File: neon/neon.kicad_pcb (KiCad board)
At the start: 2 copper layers, 60 x 50 mm, 30 parts, among them J1 V3V3-VIO, J2 V3V3-GND, J3 V3V3-GND, J4 V3V3-GND, J5 VBUS-VCC, U1 FT4232H_module, U2 A, U3 B, U4 C, U5 D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

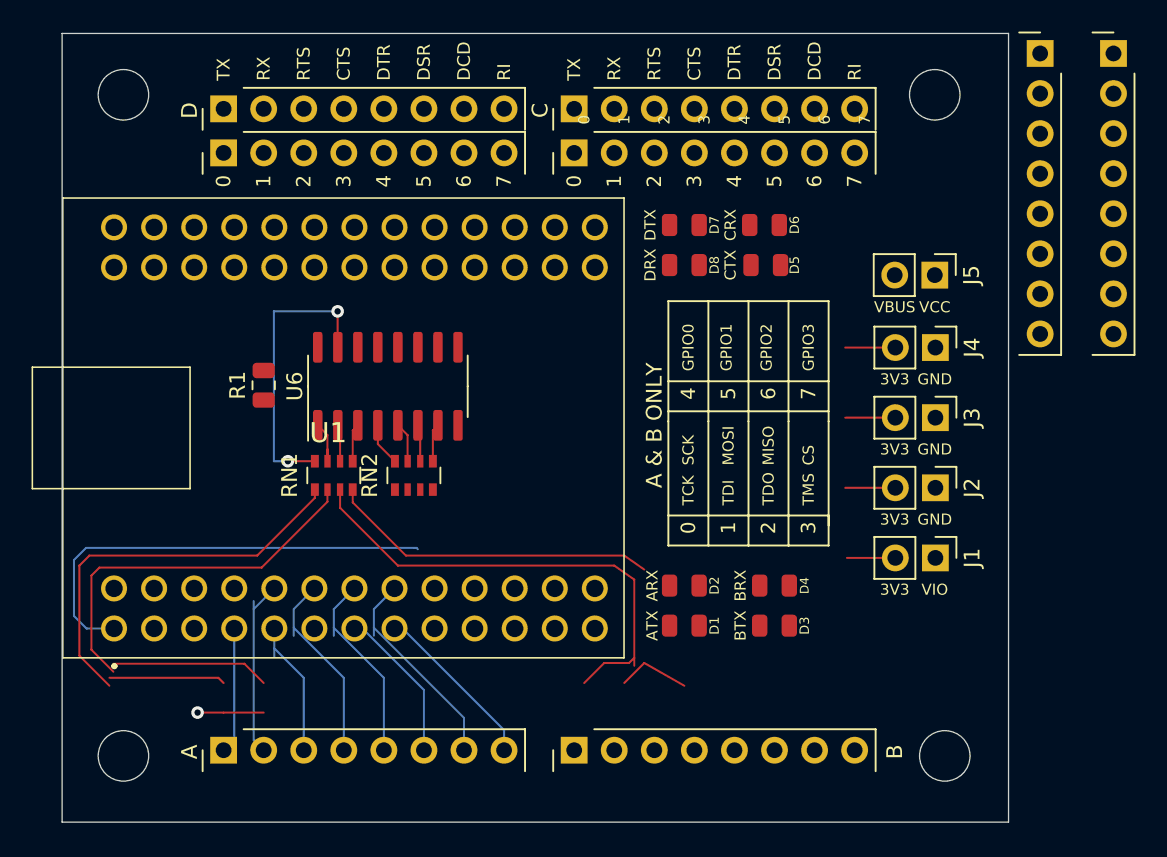
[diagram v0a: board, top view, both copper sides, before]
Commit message: All sniffers on PCB
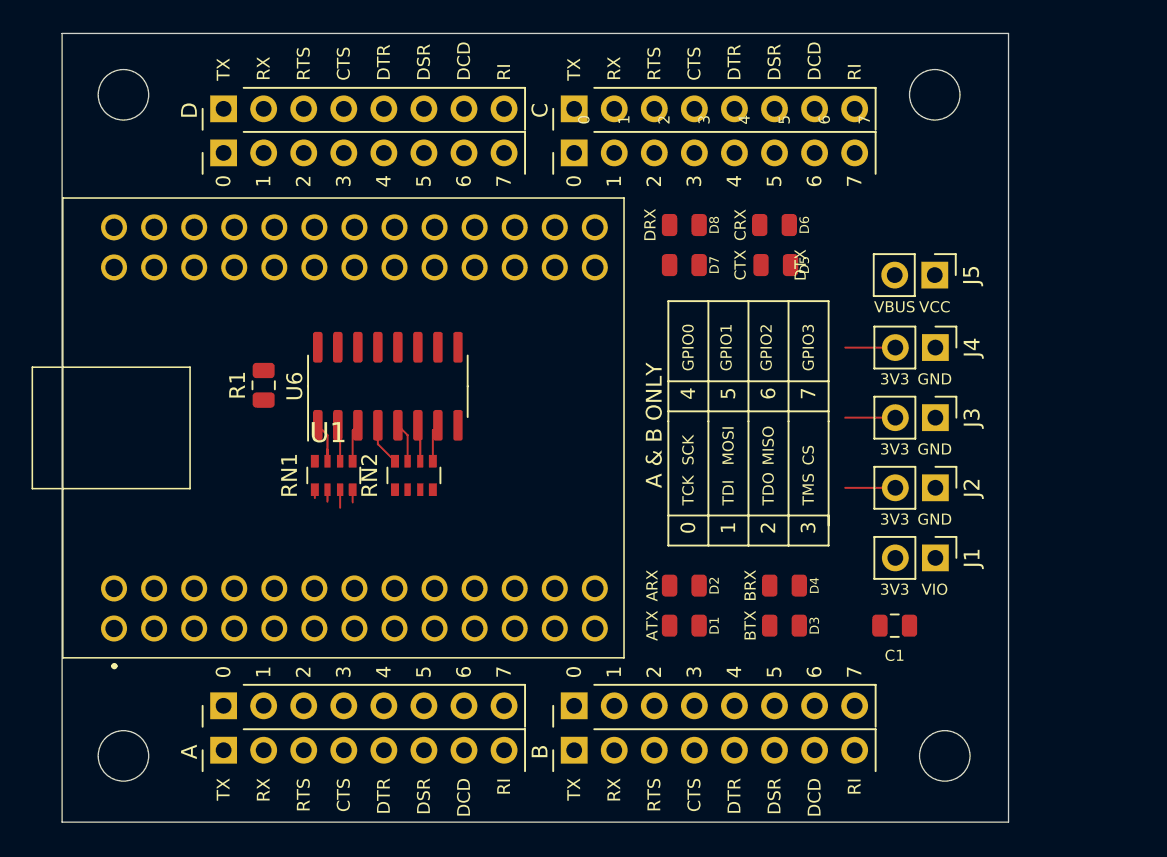
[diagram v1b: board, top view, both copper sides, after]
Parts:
- added C1: 100nF, Capacitor_SMD:C_0805_2012Metric, F.Cu at (168.3, 117.5)
- moved S3 66.3 mm to (125.7, 122.6), turned to 90 degrees
- moved S4 53.7 mm to (148.0, 122.6), turned to 90 degrees
- moved D7 2.54 mm to (154.9, 94.6)
- moved D8 2.54 mm to (154.9, 92.1)
- moved D5 0.64 mm to (160.7, 94.6)
- moved D3 0.63 mm to (161.3, 117.5)
- moved D4 0.63 mm to (161.3, 114.9)
- moved D6 0.63 mm to (160.7, 92.1)
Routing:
- net Net-(D2-Pad2): track 34.4 -> 0.77 mm
- net Net-(D1-Pad2): track 33.0 -> 0.53 mm
- net V3V3: track 41.2 -> 9.53 mm
- net Net-(D3-Pad2): track 30.9 -> 1.15 mm
- net Net-(D4-Pad2): track 25.7 -> 0.81 mm
- net Net-(RN1-Pad8): track 18.4 -> 0.02 mm, vias 2 -> 0
- net /FT4232H.sch/AD6: track 13.7 -> 0.00 mm
- net /FT4232H.sch/AD4: track 12.6 -> 0.00 mm
- net /FT4232H.sch/AD3: track 12.6 -> 0.00 mm
- net /FT4232H.sch/AD7: track 11.9 -> 0.00 mm
- net /FT4232H.sch/AD1: track 11.8 -> 0.00 mm
- net /FT4232H.sch/AD5: track 10.0 -> 0.00 mm
- net /FT4232H.sch/AD2: track 9.00 -> 0.00 mm
- net /FT4232H.sch/AD0: track 8.50 -> 0.00 mm
- net GND: track 4.19 -> 0.00 mm, vias 1 -> 0

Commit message: Fixes
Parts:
- moved D6 0.63 mm to (161.3, 92.1)
- moved D5 0.51 mm to (161.2, 94.6)
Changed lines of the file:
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@@
     (tags "resistor array")
     (attr smd)
-    (fp_text reference RN1 (at 0 -2.8 90) (layer F.SilkS)
-      (effects (font (size 1 1) (thickness 0.15)))
+    (fp_text reference RN1 (at 0 -2.159 90) (layer F.SilkS)
+      (effects (font (size 0.7 0.7) (thickness 0.15)))
     )
     (fp_text value 330 (at 0 2.8 90) (layer F.Fab)
@@
     (tags "resistor array")
     (attr smd)
-    (fp_text reference RN2 (at 0 -2.8 90) (layer F.SilkS)
-      (effects (font (size 1 1) (thickness 0.15)))
+    (fp_text reference RN2 (at 0 -2.159 90) (layer F.SilkS)
+      (effects (font (size 0.7 0.7) (thickness 0.15)))
     )
     (fp_text value 330 (at 0 2.8 90) (layer F.Fab)
@@
   )
   (module neon_footprints:LED_0805_2012Metric (layer F.Cu)
-    (at 160.655 92.075 180)
+    (at 161.29 92.075 180)
     (descr "LED SMD 0805 (2012 Metric), square (rectangular) end terminal, IPC_7351 nominal, (Body size source: https://docs.google.com/spreadsheets/d/1BsfQQcO9C6DZCsRaXUlFlo91Tg2WpOkGARC1WS5S8t0/edit?usp=sharing), generated with kicad-footprint-generator")
     (tags diode)
@@
   )
   (module neon_footprints:LED_0805_2012Metric (layer F.Cu)
-    (at 160.735 94.615 180)
+    (at 161.243 94.615 180)
     (descr "LED SMD 0805 (2012 Metric), square (rectangular) end terminal, IPC_7351 nominal, (Body size source: https://docs.google.com/spreadsheets/d/1BsfQQcO9C6DZCsRaXUlFlo91Tg2WpOkGARC1WS5S8t0/edit?usp=sharing), generated with kicad-footprint-generator")
     (tags diode)
@@
     (tags "SOIC SO")
     (attr smd)
-    (fp_text reference U6 (at 0 -5.9 90) (layer F.SilkS)
-      (effects (font (size 1 1) (thickness 0.15)))
+    (fp_text reference U6 (at 0.065 -5.588 90) (layer F.SilkS)
+      (effects (font (size 0.7 0.7) (thickness 0.15)))
     )
     (fp_text value 74HC595 (at 0 5.9 90) (layer F.Fab)
@@
     (tags resistor)
     (attr smd)
-    (fp_text reference R1 (at 0 -1.65 90) (layer F.SilkS)
-      (effects (font (size 1 1) (thickness 0.15)))
+    (fp_text reference R1 (at 0 -1.524 90) (layer F.SilkS)
+      (effects (font (size 0.7 0.7) (thickness 0.15)))
     )
     (fp_text value 10k (at 0 1.65 90) (layer F.Fab)
@@
     (effects (font (size 0.7112 0.7112) (thickness 0.175)))
   )
-  (gr_text CRX (at 158.496 92.075 90) (layer F.SilkS)
+  (gr_text CRX (at 159.004 92.075 90) (layer F.SilkS)
     (effects (font (size 0.7112 0.7112) (thickness 0.175)))
   )
@@
     (effects (font (size 0.7112 0.7112) (thickness 0.175)))
   )
-  (gr_text DTX (at 162.306 94.615 90) (layer F.SilkS)
+  (gr_text DTX (at 152.781 94.615 90) (layer F.SilkS)
     (effects (font (size 0.7112 0.7112) (thickness 0.175)))
   )
-  (gr_text CTX (at 158.496 94.615 90) (layer F.SilkS)
+  (gr_text CTX (at 159.004 94.615 90) (layer F.SilkS)
     (effects (font (size 0.7112 0.7112) (thickness 0.175)))
   )

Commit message: Problems fixes
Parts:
- moved C1 0.64 mm to (168.3, 118.1)
- moved J2 0.64 mm to (170.9, 109.4)
- moved J4 0.64 mm to (170.9, 100.5)
- moved J5 0.64 mm to (170.8, 95.9)
- moved J1 0.63 mm to (170.9, 113.8)
- moved J3 0.63 mm to (170.9, 104.9)
- renumbered U4 to U2, U2 to U4

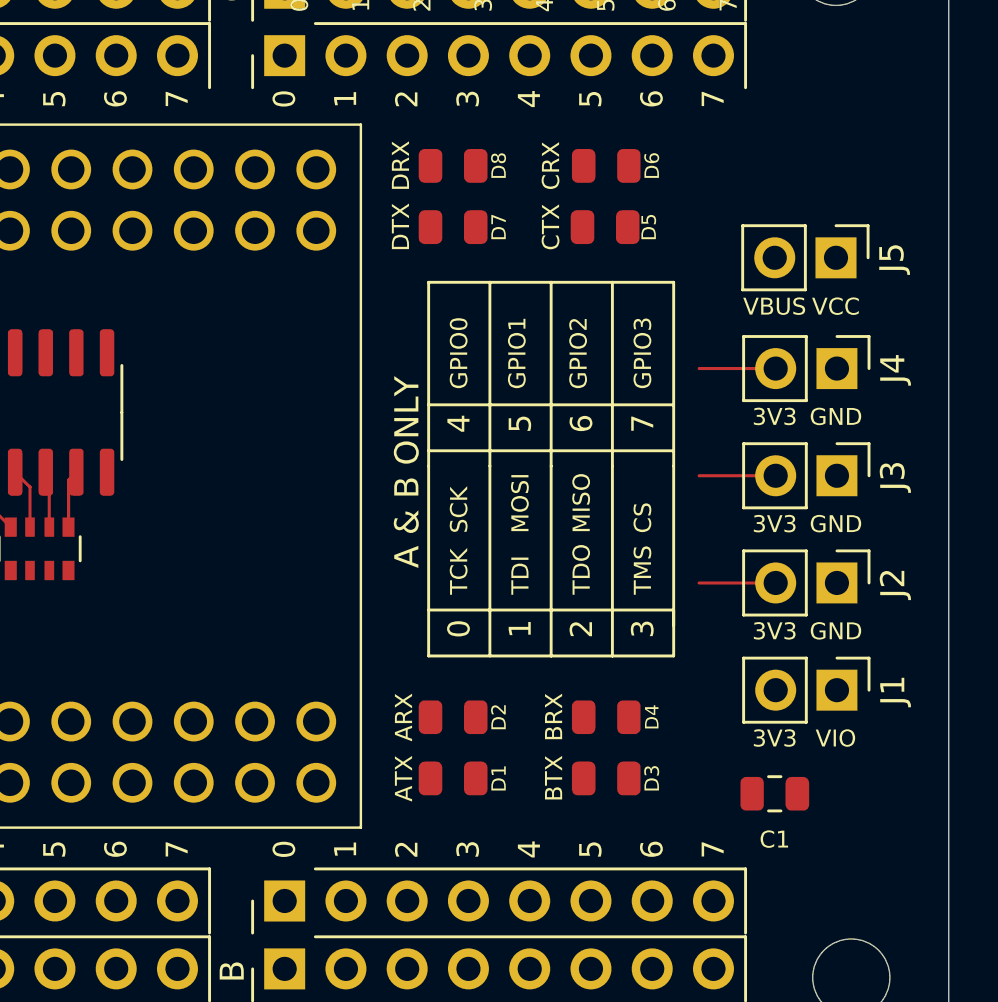
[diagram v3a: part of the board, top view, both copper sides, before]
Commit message: Center things & rotate J1 & J5
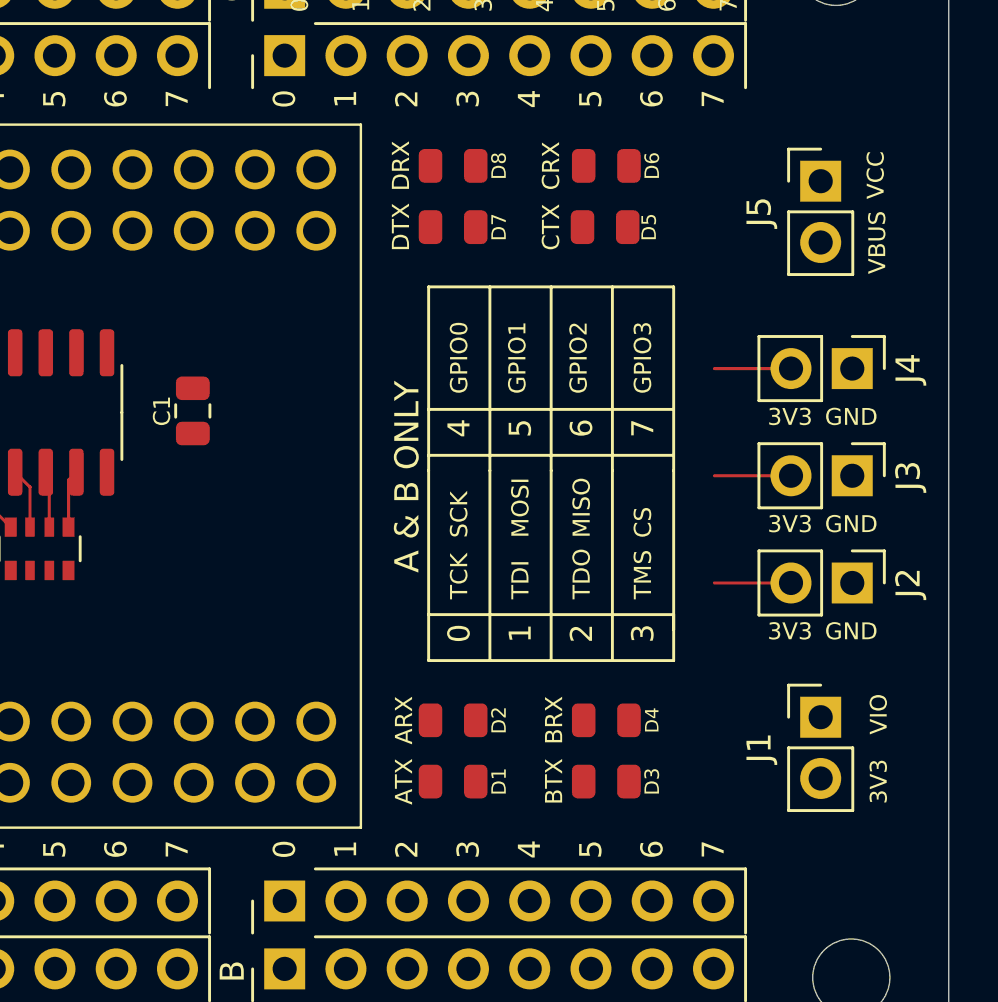
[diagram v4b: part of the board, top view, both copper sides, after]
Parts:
- moved C1 28.9 mm to (144.1, 102.2), turned to 270 degrees
- moved J5 3.24 mm to (170.2, 92.7), turned to 0 degrees
- moved J1 1.31 mm to (170.2, 114.9), turned to 0 degrees
- moved J2 0.63 mm to (171.5, 109.4)
- moved J3 0.63 mm to (171.5, 104.9)
- moved J4 0.63 mm to (171.5, 100.5)
- moved D1 0.13 mm to (154.9, 117.6)
- moved D3 0.13 mm to (161.3, 117.6)
- moved D2 0.13 mm to (154.9, 115.1)
- moved D4 0.13 mm to (161.3, 115.1)

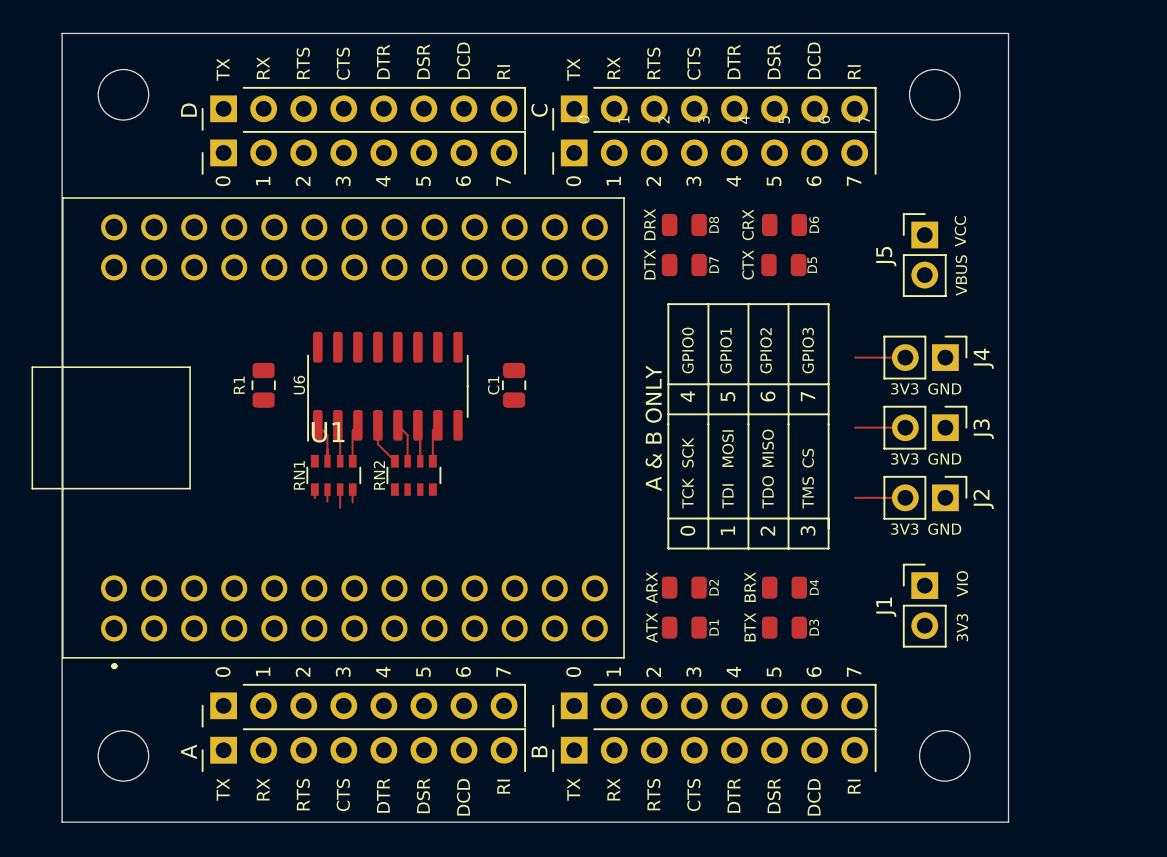
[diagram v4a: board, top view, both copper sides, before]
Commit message: A, B, C & D distances
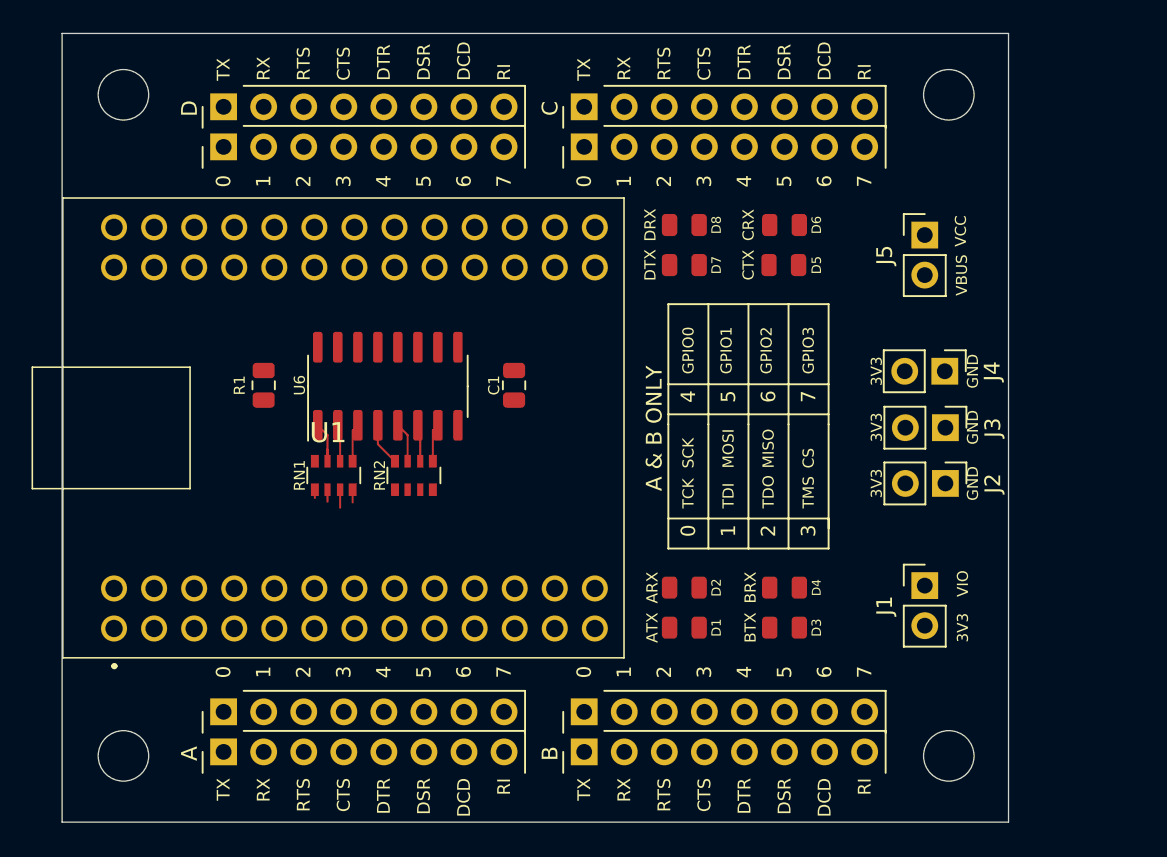
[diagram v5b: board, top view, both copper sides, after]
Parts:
- moved J2 0.91 mm to (171.5, 108.5)
- moved H2 0.89 mm to (171.7, 83.8)
- moved J4 0.87 mm to (171.4, 101.3)
- moved S1 0.74 mm to (148.6, 87.1)
- moved S4 0.74 mm to (148.6, 122.9)
- moved U2 0.65 mm to (148.6, 84.6)
- moved U3 0.64 mm to (148.6, 125.5)
- moved S2 0.38 mm to (125.7, 87.1)
- moved S3 0.38 mm to (125.7, 122.9)
- moved H4 0.25 mm to (171.7, 125.7)
- moved U5 0.13 mm to (125.7, 84.6)
- moved U4 0.11 mm to (125.7, 125.5)
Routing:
- net V3V3: track 9.52 -> 0.00 mm

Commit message: Add 3x2 connector for GND&3v3
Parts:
- removed J3, J4: V3V3-GND, Connector_PinHeader_2.54mm:PinHeader_1x02_P2.54mm_Vertical
- J2: value V3V3-GND -> 3xV3V3-GND; footprint Connector_PinHeader_2.54mm:PinHeader_1x02_P2.54mm_Vertical -> Connector_PinHeader_2.54mm:PinHeader_2x03_P2.54mm_Vertical
- moved J2 6.57 mm to (169.0, 102.4), turned to 0 degrees
- moved J5 0.51 mm to (170.2, 92.2)
- moved J1 0.13 mm to (170.2, 115.1)

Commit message: Bigger letters & remove random dot
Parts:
- added D9: LED, neon_footprints:LED_0805_2012Metric, F.Cu at (119.4, 88.9)
- added R2: 100, Resistor_SMD:R_0805_2012Metric, F.Cu at (119.4, 98.4)
- moved C1 16.7 mm to (128.3, 107.6)
- moved RN1 7.00 mm to (139.7, 108.3), turned to 180 degrees
- moved RN2 5.07 mm to (139.7, 103.3), turned to 180 degrees
- moved U6 3.34 mm to (134.1, 104.9), turned to 180 degrees
- moved D3 2.54 mm to (163.8, 117.7)
- moved D4 2.54 mm to (163.8, 115.2)
- moved D6 2.54 mm to (163.8, 92.1)
- moved D5 2.54 mm to (163.8, 94.6)
- moved D1 1.28 mm to (156.2, 117.7)
- moved D2 1.28 mm to (156.2, 115.2)
- moved D7 1.27 mm to (156.2, 94.6)
- moved D8 1.27 mm to (156.2, 92.1)
- moved J1 0.38 mm to (170.6, 115.1)
- moved J2 0.38 mm to (169.4, 102.4)
- moved J5 0.38 mm to (170.6, 92.2)
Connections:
- J5 pad 1: /FT4232H.sch/VCC -> /FT4232H.sch/VBUS
- J5 pad 2: /FT4232H.sch/VBUS -> /FT4232H.sch/VCC
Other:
- board text added: "A"
- board text added: "B"
- board text added: "C"
- board text added: "D"
- board text removed: "ARX"
- board text removed: "ATX"
- board text removed: "BRX"
- board text removed: "BTX"
- board text removed: "CRX"
- board text removed: "CTX"
- board text removed: "DRX"
- board text removed: "DTX"
